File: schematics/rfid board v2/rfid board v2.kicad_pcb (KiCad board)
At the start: 2 copper layers, 62.2 x 47.6 mm, 18 parts, among them J1 RFID_RJ45, J2 CONN_15, J3 CONN_15, J5 POWER_JACK, J6 CONN_02, K1 SANYOU_SRD_Form_C, Q1 TRANS_NPN-P2N2222A, U1 VREG_3V3

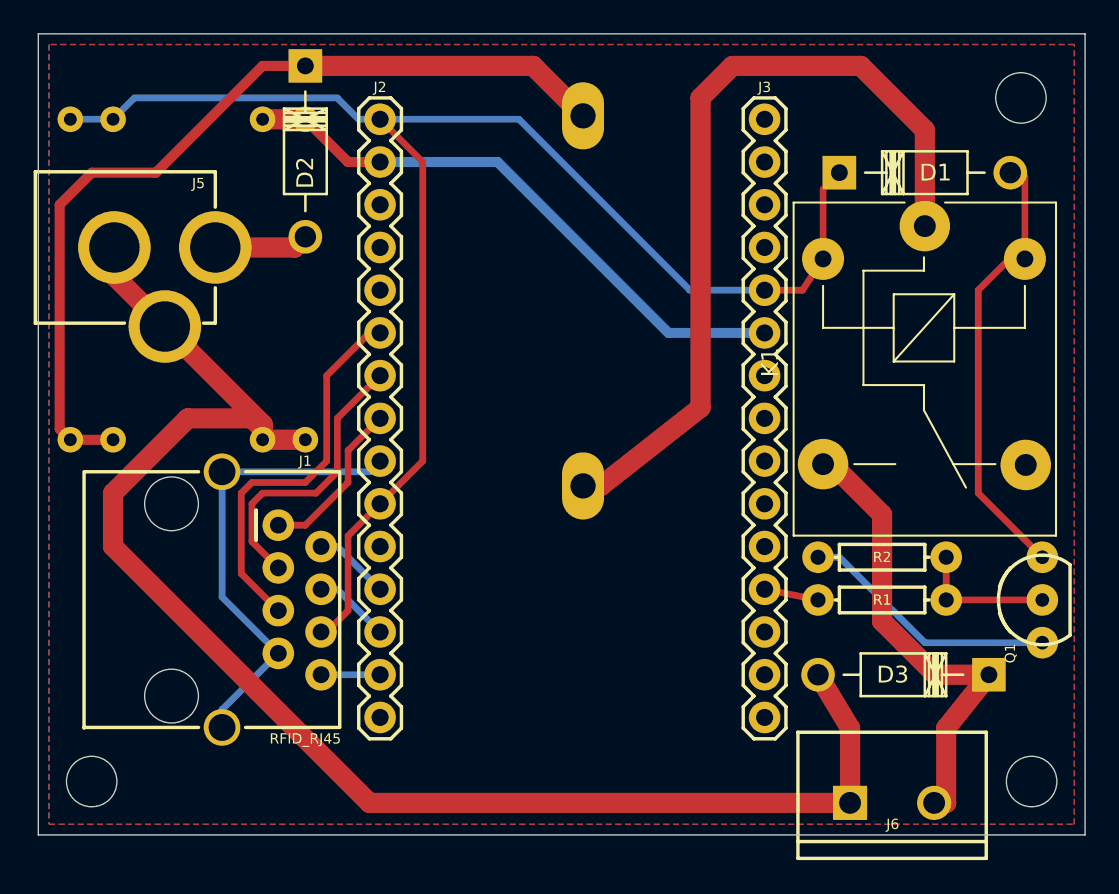
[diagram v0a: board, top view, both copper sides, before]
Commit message: Made vreg 3.3V component pads a little larger
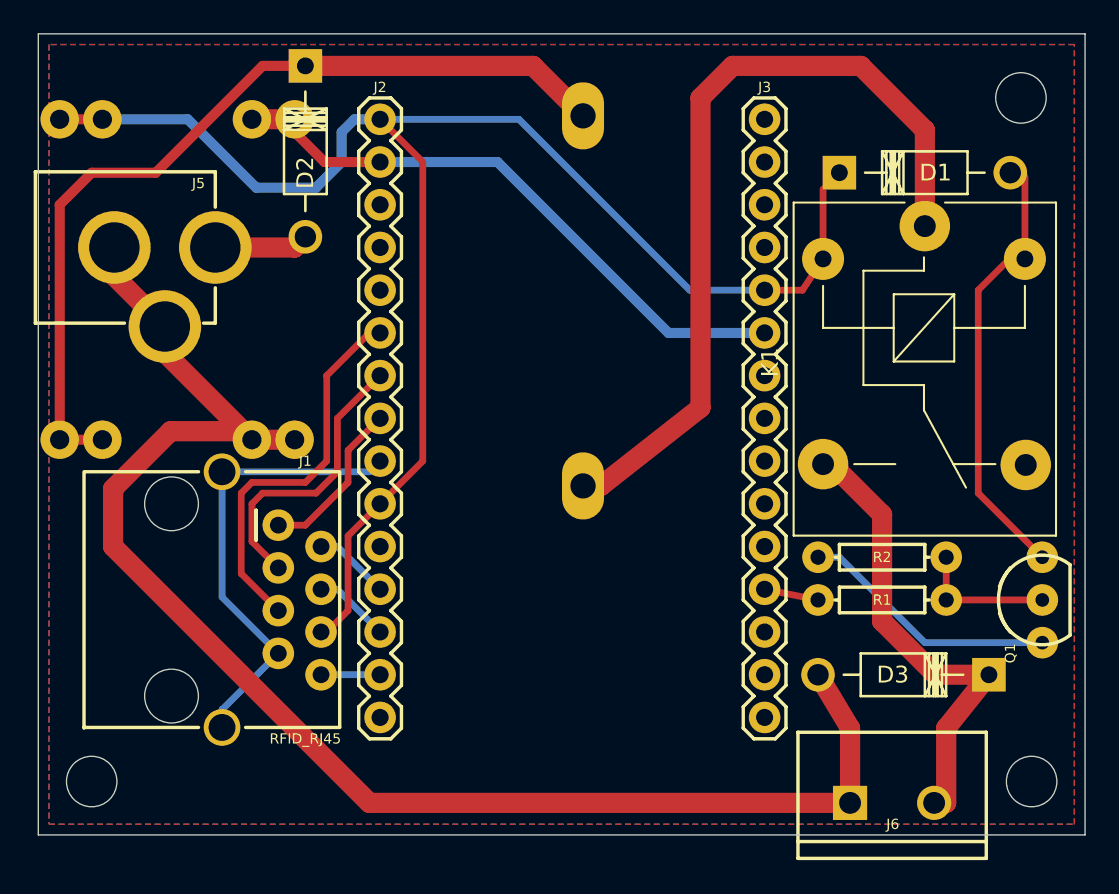
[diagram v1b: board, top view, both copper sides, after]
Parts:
- removed G***: LOGO, Nightowl logos:nightowl logo
- moved U1 0.64 mm to (39.4, 19.1)
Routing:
- net +3V3: track 91.7 -> 95.7 mm
- net Net-(D3-Pad2): track 91.3 -> 89.6 mm
- net GND: track 79.4 -> 80.5 mm

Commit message: Updated components to match new libaries
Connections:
- J2 pad 11: (no net) -> Net-(J2-Pad11)
- J2 pad 15: (no net) -> Net-(J2-Pad15)
- J2 pad 3: (no net) -> Net-(J2-Pad3)
- J2 pad 4: (no net) -> Net-(J2-Pad4)
- J2 pad 5: (no net) -> Net-(J2-Pad5)
- J3 pad 1: (no net) -> Net-(J3-Pad1)
- J3 pad 10: (no net) -> Net-(J3-Pad10)
- J3 pad 11: (no net) -> Net-(J3-Pad11)
- J3 pad 13: (no net) -> Net-(J3-Pad13)
- J3 pad 14: (no net) -> Net-(J3-Pad14)
- J3 pad 15: (no net) -> Net-(J3-Pad15)
- J3 pad 2: (no net) -> Net-(J3-Pad2)
- J3 pad 3: (no net) -> Net-(J3-Pad3)
- J3 pad 4: (no net) -> Net-(J3-Pad4)
- J3 pad 7: (no net) -> Net-(J3-Pad7)
- J3 pad 8: (no net) -> Net-(J3-Pad8)
- J3 pad 9: (no net) -> Net-(J3-Pad9)
- K1 pad 4: (no net) -> Net-(K1-Pad4)
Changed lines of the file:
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@@
-(kicad_pcb (version 4) (host pcbnew 4.0.2+dfsg1-stable)
+(kicad_pcb (version 20171130) (host pcbnew 5.0.2-5.fc29)
   (general
-    (links 39)
-    (no_connects 0)
-    (area 19.235 13.9245 88.21457 65.66626)
     (thickness 1.6)
     (drawings 24)
@@
     (zones 0)
     (modules 17)
-    (nets 17)
+    (nets 35)
   )
   (page A4)
@@
     (pad_drill 1.016)
     (pad_to_mask_clearance 0.2)
+    (solder_mask_min_width 0.25)
     (aux_axis_origin 0 0)
     (visible_elements FFFFFF7F)
@@
       (usegerberextensions false)
       (usegerberattributes true)
+      (usegerberadvancedattributes false)
+      (creategerberjobfile false)
       (excludeedgelayer false)
       (linewidth 0.100000)
@@
       (hpglpennumber 1)
       (hpglpenspeed 20)
-      (hpglpendiameter 15)
-      (hpglpenoverlay 2)
+      (hpglpendiameter 15.000000)
       (psnegative false)
       (psa4output false)
@@
       (drillshape 0)
       (scaleselection 1)
-      (outputdirectory gerbers/))
+      (outputdirectory "gerbers/"))
   )
   (net 0 "")
@@
   (net 15 /SDA)
   (net 16 /RST)
+  (net 17 "Net-(K1-Pad4)")
+  (net 18 "Net-(J3-Pad1)")
+  (net 19 "Net-(J3-Pad2)")
+  (net 20 "Net-(J3-Pad3)")
+  (net 21 "Net-(J3-Pad4)")
+  (net 22 "Net-(J3-Pad7)")
+  (net 23 "Net-(J3-Pad8)")
+  (net 24 "Net-(J3-Pad9)")
+  (net 25 "Net-(J3-Pad10)")
+  (net 26 "Net-(J3-Pad11)")
+  (net 27 "Net-(J3-Pad13)")
+  (net 28 "Net-(J3-Pad14)")
+  (net 29 "Net-(J3-Pad15)")
+  (net 30 "Net-(J2-Pad3)")
+  (net 31 "Net-(J2-Pad4)")
+  (net 32 "Net-(J2-Pad5)")
+  (net 33 "Net-(J2-Pad11)")
+  (net 34 "Net-(J2-Pad15)")
   (net_class Default "This is the default net class."
     (clearance 0.2)
@@
     (add_net "Net-(D3-Pad2)")
     (add_net "Net-(F1-Pad1)")
+    (add_net "Net-(J2-Pad11)")
+    (add_net "Net-(J2-Pad15)")
+    (add_net "Net-(J2-Pad3)")
+    (add_net "Net-(J2-Pad4)")
+    (add_net "Net-(J2-Pad5)")
+    (add_net "Net-(J3-Pad1)")
+    (add_net "Net-(J3-Pad10)")
+    (add_net "Net-(J3-Pad11)")
     (add_net "Net-(J3-Pad12)")
+    (add_net "Net-(J3-Pad13)")
+    (add_net "Net-(J3-Pad14)")
+    (add_net "Net-(J3-Pad15)")
+    (add_net "Net-(J3-Pad2)")
+    (add_net "Net-(J3-Pad3)")
+    (add_net "Net-(J3-Pad4)")
+    (add_net "Net-(J3-Pad7)")
+    (add_net "Net-(J3-Pad8)")
+    (add_net "Net-(J3-Pad9)")
+    (add_net "Net-(K1-Pad4)")
     (add_net "Net-(Q1-Pad2)")
   )
@@
     (tags "RJ45 ETHERNET MAGJACK-COMPATIBLE")
     (attr virtual)
-    (fp_text reference J1 (at -0.635 -19.05 360) (layer F.SilkS)
-      (effects (font (size 0.6096 0.6096) (thickness 0.127)))
-    )
-    (fp_text value RFID_RJ45 (at 15.875 -19.05 360) (layer F.SilkS)
+    (fp_text reference J1 (at -0.635 -19.05) (layer F.SilkS)
+      (effects (font (size 0.6096 0.6096) (thickness 0.127)))
+    )
+    (fp_text value RFID_RJ45 (at 15.875 -19.05) (layer F.SilkS)
       (effects (font (size 0.6096 0.6096) (thickness 0.127)))
     )
@@
     (pad 3 thru_hole circle (at 14.15 6.05) (size 3 3) (drill 1.3) (layers *.Cu *.Mask)
       (net 5 "Net-(D3-Pad1)"))
-    (pad 4 thru_hole circle (at 14.2 -6) (size 3 3) (drill 1.3) (layers *.Cu *.Mask))
+    (pad 4 thru_hole circle (at 14.2 -6) (size 3 3) (drill 1.3) (layers *.Cu *.Mask)
+      (net 17 "Net-(K1-Pad4)"))
     (pad 5 thru_hole circle (at 1.95 -5.95) (size 2.5 2.5) (drill 1) (layers *.Cu *.Mask)
       (net 1 "Net-(D1-Pad2)"))
@@
     (tags "PLATED THROUGH HOLE -15 PIN")
     (attr virtual)
-    (fp_text reference J2 (at -1.905 0 360) (layer F.SilkS)
+    (fp_text reference J2 (at -1.905 0) (layer F.SilkS)
       (effects (font (size 0.6096 0.6096) (thickness 0.127)))
     )
@@
       (net 9 GND) (solder_mask_margin 0.1016))
     (pad 3 thru_hole circle (at 5.08 0 270) (size 1.8796 1.8796) (drill 1.016) (layers *.Cu *.Mask)
-      (solder_mask_margin 0.1016))
+      (net 30 "Net-(J2-Pad3)") (solder_mask_margin 0.1016))
     (pad 4 thru_hole circle (at 7.62 0 270) (size 1.8796 1.8796) (drill 1.016) (layers *.Cu *.Mask)
-      (solder_mask_margin 0.1016))
+      (net 31 "Net-(J2-Pad4)") (solder_mask_margin 0.1016))
     (pad 5 thru_hole circle (at 10.16 0 270) (size 1.8796 1.8796) (drill 1.016) (layers *.Cu *.Mask)
-      (solder_mask_margin 0.1016))
+      (net 32 "Net-(J2-Pad5)") (solder_mask_margin 0.1016))
     (pad 6 thru_hole circle (at 12.7 0 270) (size 1.8796 1.8796) (drill 1.016) (layers *.Cu *.Mask)
       (net 11 /MOSI) (solder_mask_margin 0.1016))
@@
       (net 10 +3V3) (solder_mask_margin 0.1016))
     (pad 11 thru_hole circle (at 25.4 0 270) (size 1.8796 1.8796) (drill 1.016) (layers *.Cu *.Mask)
-      (solder_mask_margin 0.1016))
+      (net 33 "Net-(J2-Pad11)") (solder_mask_margin 0.1016))
     (pad 12 thru_hole circle (at 27.94 0 270) (size 1.8796 1.8796) (drill 1.016) (layers *.Cu *.Mask)
       (net 13 /BUZZER) (solder_mask_margin 0.1016))
@@
       (net 16 /RST) (solder_mask_margin 0.1016))
     (pad 15 thru_hole circle (at 35.56 0 270) (size 1.8796 1.8796) (drill 1.016) (layers *.Cu *.Mask)
-      (solder_mask_margin 0.1016))
+      (net 34 "Net-(J2-Pad15)") (solder_mask_margin 0.1016))
   )
   (module Connectors:1X15 (layer F.Cu)
@@
     (tags "PLATED THROUGH HOLE -15 PIN")
     (attr virtual)
-    (fp_text reference J3 (at -1.905 0 360) (layer F.SilkS)
+    (fp_text reference J3 (at -1.905 0) (layer F.SilkS)
       (effects (font (size 0.6096 0.6096) (thickness 0.127)))
     )
@@
     (fp_line (start 34.29 0.635) (end 34.925 1.27) (layer F.SilkS) (width 0.2032))
     (pad 1 thru_hole circle (at 0 0 270) (size 1.8796 1.8796) (drill 1.016) (layers *.Cu *.Mask)
-      (solder_mask_margin 0.1016))
+      (net 18 "Net-(J3-Pad1)") (solder_mask_margin 0.1016))
     (pad 2 thru_hole circle (at 2.54 0 270) (size 1.8796 1.8796) (drill 1.016) (layers *.Cu *.Mask)
-      (solder_mask_margin 0.1016))
+      (net 19 "Net-(J3-Pad2)") (solder_mask_margin 0.1016))
     (pad 3 thru_hole circle (at 5.08 0 270) (size 1.8796 1.8796) (drill 1.016) (layers *.Cu *.Mask)
-      (solder_mask_margin 0.1016))
+      (net 20 "Net-(J3-Pad3)") (solder_mask_margin 0.1016))
     (pad 4 thru_hole circle (at 7.62 0 270) (size 1.8796 1.8796) (drill 1.016) (layers *.Cu *.Mask)
-      (solder_mask_margin 0.1016))
+      (net 21 "Net-(J3-Pad4)") (solder_mask_margin 0.1016))
     (pad 5 thru_hole circle (at 10.16 0 270) (size 1.8796 1.8796) (drill 1.016) (layers *.Cu *.Mask)
       (net 10 +3V3) (solder_mask_margin 0.1016))
@@
       (net 9 GND) (solder_mask_margin 0.1016))
     (pad 7 thru_hole circle (at 15.24 0 270) (size 1.8796 1.8796) (drill 1.016) (layers *.Cu *.Mask)
-      (solder_mask_margin 0.1016))
+      (net 22 "Net-(J3-Pad7)") (solder_mask_margin 0.1016))
     (pad 8 thru_hole circle (at 17.78 0 270) (size 1.8796 1.8796) (drill 1.016) (layers *.Cu *.Mask)
-      (solder_mask_margin 0.1016))
+      (net 23 "Net-(J3-Pad8)") (solder_mask_margin 0.1016))
     (pad 9 thru_hole circle (at 20.32 0 270) (size 1.8796 1.8796) (drill 1.016) (layers *.Cu *.Mask)
-      (solder_mask_margin 0.1016))
+      (net 24 "Net-(J3-Pad9)") (solder_mask_margin 0.1016))
     (pad 10 thru_hole circle (at 22.86 0 270) (size 1.8796 1.8796) (drill 1.016) (layers *.Cu *.Mask)
-      (solder_mask_margin 0.1016))
+      (net 25 "Net-(J3-Pad10)") (solder_mask_margin 0.1016))
     (pad 11 thru_hole circle (at 25.4 0 270) (size 1.8796 1.8796) (drill 1.016) (layers *.Cu *.Mask)
-      (solder_mask_margin 0.1016))
+      (net 26 "Net-(J3-Pad11)") (solder_mask_margin 0.1016))
     (pad 12 thru_hole circle (at 27.94 0 270) (size 1.8796 1.8796) (drill 1.016) (layers *.Cu *.Mask)
       (net 7 "Net-(J3-Pad12)") (solder_mask_margin 0.1016))
     (pad 13 thru_hole circle (at 30.48 0 270) (size 1.8796 1.8796) (drill 1.016) (layers *.Cu *.Mask)
-      (solder_mask_margin 0.1016))
+      (net 27 "Net-(J3-Pad13)") (solder_mask_margin 0.1016))
     (pad 14 thru_hole circle (at 33.02 0 270) (size 1.8796 1.8796) (drill 1.016) (layers *.Cu *.Mask)
-      (solder_mask_margin 0.1016))
+      (net 28 "Net-(J3-Pad14)") (solder_mask_margin 0.1016))
     (pad 15 thru_hole circle (at 35.56 0 270) (size 1.8796 1.8796) (drill 1.016) (layers *.Cu *.Mask)
-      (solder_mask_margin 0.1016))
+      (net 29 "Net-(J3-Pad15)") (solder_mask_margin 0.1016))
   )
   (module Connectors:POWER_JACK_PTH (layer F.Cu)
@@
     (tags "DC BARREL POWER JACK/CONNECTOR PTH")
     (attr virtual)
-    (fp_text reference J5 (at -3.81 -12.7 360) (layer F.SilkS)
-      (effects (font (size 0.6096 0.6096) (thickness 0.127)))
-    )
-    (fp_text value POWER_JACK (at 5.207 -5.08 360) (layer F.SilkS) hide
-      (effects (font (size 0.6096 0.6096) (thickness 0.127)))
-    )
+    (fp_text reference J5 (at -3.81 -12.7) (layer F.SilkS)
+      (effects (font (size 0.6096 0.6096) (thickness 0.127)))
+    )
+    (fp_text value POWER_JACK (at 5.207 -5.08) (layer F.SilkS) hide
+      (effects (font (size 0.6096 0.6096) (thickness 0.127)))
+    )
